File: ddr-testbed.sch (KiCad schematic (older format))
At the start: 23 parts, among them J1 ddr4-sodimm-edge-connector, U1 MT53E256M16D1

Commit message: Add changes refering to Xilinx documentation
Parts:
- added C?: C_10n_0402, antmicro-footprints:0402-cap, symbol antmicroCapacitors0402:C_10n_0402
- added R? (x4): R_0R_0402, antmicro-footprints:0402-res, symbol antmicroResistors0402:R_0R_0402
- added R? (x19): R_40R2_0402, antmicro-footprints:0402-res, symbol antmicroResistors0402:R_40R2_0402
- added R?: R_80R6_0402, antmicro-footprints:0402-res, symbol antmicroResistors0402:R_80R6_0402
- added R?: R_4k7_0402, antmicro-footprints:0402-res, symbol antmicroResistors0402:R_4k7_0402
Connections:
- net CK0_C_A is gone; now on net CK0_C: U1.J9 (CK_C_A)
- net CK0_C_B is gone; now on net CK1_C: U1.P9 (CK_C_B)
- net CK0_T_A is gone; now on net CK0_T: U1.J8 (CK_T_A)
- net CK0_T_B is gone; now on net CK1_T: U1.P8 (CK_T_B)
- net ODT0_A is gone; now on net GND: U1.G2 (ODT_CA_A)
- net ODT0_B is gone; now on net GND: U1.T2 (ODT_CA_B)
- net VTT is gone; now on net GND: R?.1, R?.1, R?.1, R?.1, R?.1, R?.1, R?.1, R?.1, R?.1, R?.1, R?.1, R?.1, R?.1, R?.1
- net CA0_A: now also R?.1
- net CA0_B: now also J1.146, R?.1; no longer J1.127
- net CA1_A: now also R?.1
- net CA1_B: now also J1.120, R?.1; no longer J1.122
- net CA2_A: now also R?.1
- net CA2_B: now also J1.119, R?.1; no longer J1.125
- net CA3_A: now also R?.1
- net CA3_B: now also J1.158, R?.1; no longer J1.121
- net CA4_A: now also R?.1
- net CA4_B: now also J1.151, R?.1; no longer J1.146
- net CA5_A: now also R?.1
- net CA5_B: now also J1.156, R?.1; no longer J1.120
- net CK0_C: now also R?.1
- net CK0_T: now also R?.1
- net CK1_C: now also R?.1
- net CK1_T: now also R?.1
- net CKE0_A: now also R?.1
- net CKE0_B: now also R?.1
- net CS0_N_A: now also R?.1
- net CS0_N_B: now also R?.1
- net DDRVCC: now also C?.1, R?.1
- net GND: now also C?.2, R?.2, R?.2, R?.2, R?.2, R?.2, R?.2, R?.2, R?.2, R?.2, R?.2, R?.2, R?.2, R?.2, R?.2, R?.2, R?.2, R?.2, R?.2, R?.2, R?.2
- net RESET_CONN_N: now also R?.1
- net CKE_0: now reaches J1.109
- net CKE_0: now also R?.2, R?.2, R?.2
- new net CKE_0_A: R?.1
- new net CKE_0_B: R?.1
- new net CS_0_N: R?.1, R?.2, R?.2
- no-connect marks 16 -> 15
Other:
- note added: "Pull up or pull down?\n"
- note added: "TODO: Replace with R_40"
- note added: "TODO: Replace with R_80"
- note added: "What is taht pin?"

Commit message: Add changes in pull ups and add missing components
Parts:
- removed C?: C_3p_0402, antmicro-footprints:0402-cap, symbol antmicroCapacitors0402:C_3p_0402
- removed R? (x14): R_33R_0402, antmicro-footprints:0402-res, symbol antmicroResistors0402:R_33R_0402
- removed R?: R_120R_0603, antmicro-footprints:0603-res, symbol antmicroResistors0603:R_120R_0603
- removed R?: R_39k_0402, antmicro-footprints:0402-res, symbol antmicroResistors0402:R_39k_0402
- removed R?: R_75R_0603, antmicro-footprints:0603-res, symbol antmicroResistors0603:R_75R_0603
- added C?: C_3p3_0402, antmicro-footprints:0402-res, symbol antmicroCapacitors0402:C_3p3_0402
- added R? (x4): R_0R_0402, antmicro-footprints:0402-res, symbol antmicroResistors0402:R_0R_0402
- added R? (x2): R_40R2_0402, antmicro-footprints:0402-res, symbol antmicroResistors0402:R_40R2_0402
- added R?: R_75R_0402, antmicro-footprints:0402-res, symbol antmicroResistors0402:R_75R_0402
- added R?: R_120R_0402, antmicro-footprints:0402-res, symbol antmicroResistors0402:R_120R_0402
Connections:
- net ALERT_N: now also R?.1
- net CK0_C: now also C?.1
- net CK0_T: now also C?.2
- net CK1_C: now also R?.2
- net CK1_T: now also R?.1
- net CS_0_N: now also R?.1, R?.1; no longer R?.1, R?.2
- net DDRVCC: now also R?.2
- net GND: now also R?.2, R?.2; no longer U1.G2 (ODT_CA_A), U1.T2 (ODT_CA_B)
- net MEMRST_N: now also R?.2
- net ODT0: now also R?.2
- net RESET_CONN_N: now also R?.1
- net CS_1_N: now reaches J1.157
- net CS_1_N: now also R?.1, R?.2, R?.2
- net ODT1: now reaches J1.161
- net ODT1: now also R?.2
- net VDDSPD: now reaches J1.255
- net VPP: now reaches J1.257
- net VPP: now also J1.259
- net VTT: now reaches J1.258
- new net ODT0_A: R?.1, R?.1, R?.1, U1.G2 (ODT_CA_A), U1.T2 (ODT_CA_B)
- no-connect marks 15 -> 17
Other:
- note added: "Bank adress"
- note added: "Bank group\n"
- note added: "To check"
- note removed: "?"
- note removed: "TODO: Replace with 0402"
- note removed: "TODO: Replace with 39R"
- note removed: "TODO: Replace with C_3p3"
- note removed: "TODO: Replace with R_36"
- note removed: "TODO: Replace with R_40"
- note removed: "TODO: Replace with R_80"
- note removed: "TODO: replace with 0402\n"
- moved on the sheet: C?, J1B, R?

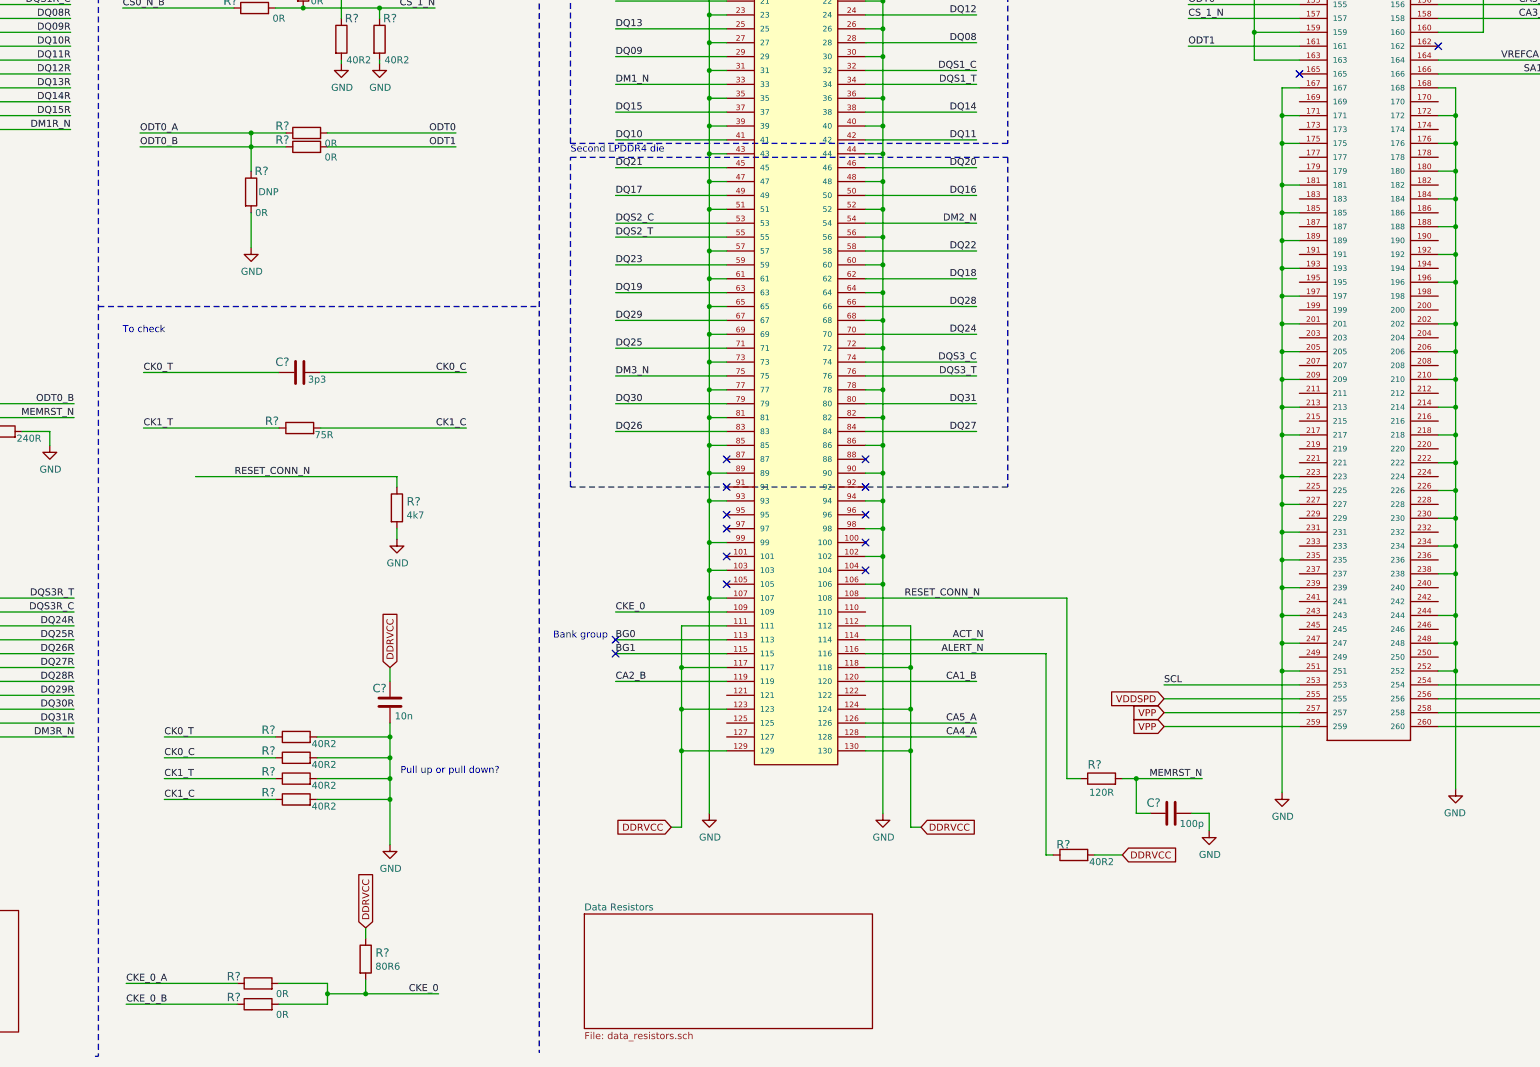
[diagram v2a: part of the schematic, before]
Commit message: Add changes around CKE pins and some notes
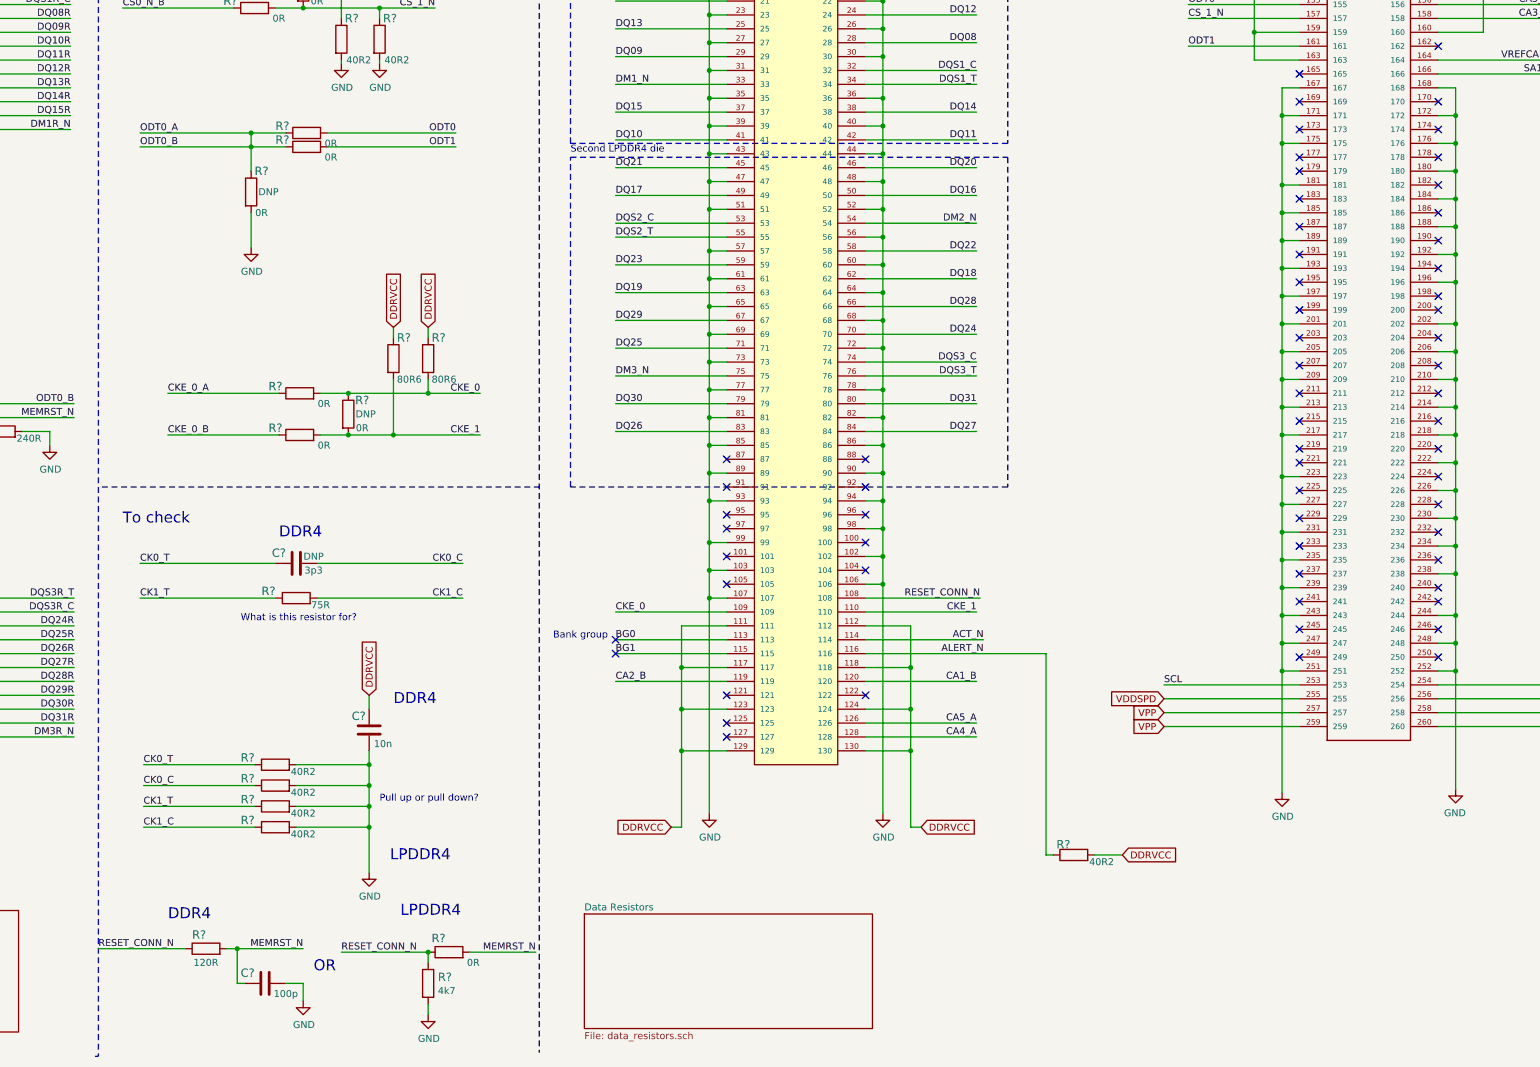
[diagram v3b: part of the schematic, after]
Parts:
- removed R? (x2): R_0R_0402, antmicro-footprints:0402-res, symbol antmicroResistors0402:R_0R_0402
- added R? (x4): R_0R_0402, antmicro-footprints:0402-res, symbol antmicroResistors0402:R_0R_0402
- added R?: R_80R6_0402, antmicro-footprints:0402-res, symbol antmicroResistors0402:R_80R6_0402
- C?: Populate (none) -> DNP
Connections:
- net CKE_0: now also R?.1, R?.2
- net CKE_0_A: now also R?.1
- net CKE_0_B: now also R?.1
- net DDRVCC: now also R?.1
- net MEMRST_N: now also R?.2
- net RESET_CONN_N: now also R?.1
- net CKE_1: now reaches J1.110
- net CKE_1: now also R?.2, R?.2, R?.2
- no-connect marks 17 -> 65
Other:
- note added: "DDR4"
- note added: "OR"
- note added: "What is this resistor for?"
- moved on the sheet: C?, R?

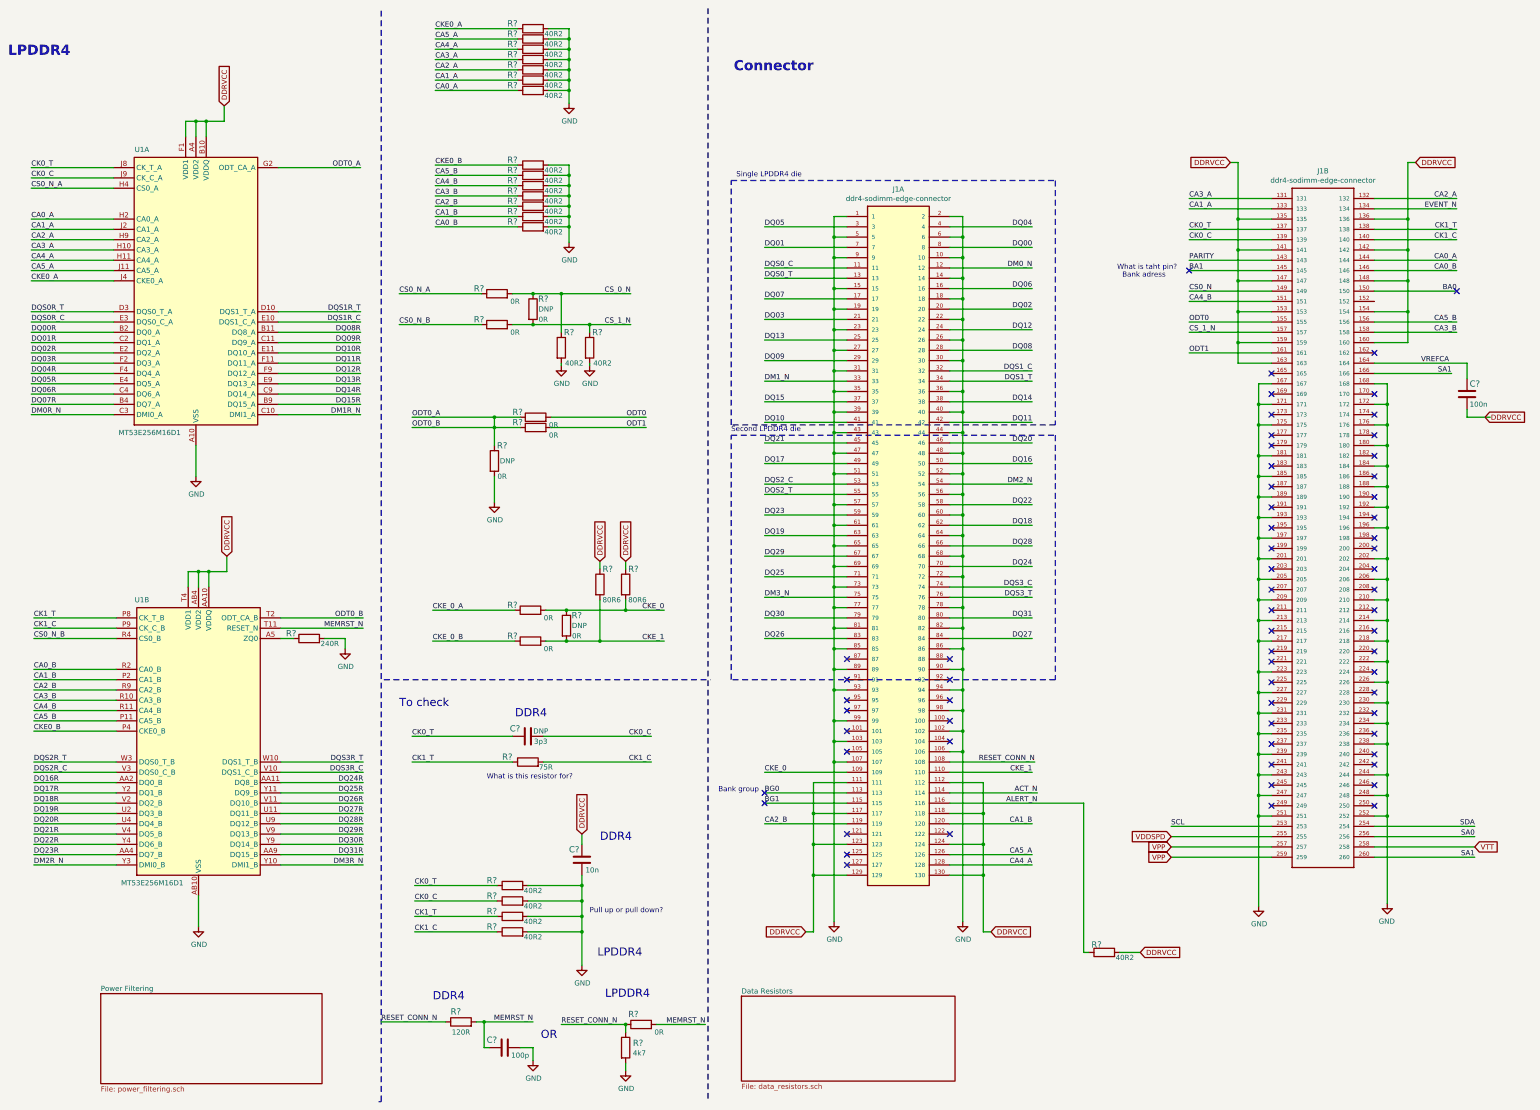
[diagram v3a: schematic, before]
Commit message: Remove data resistors sheet and add notes
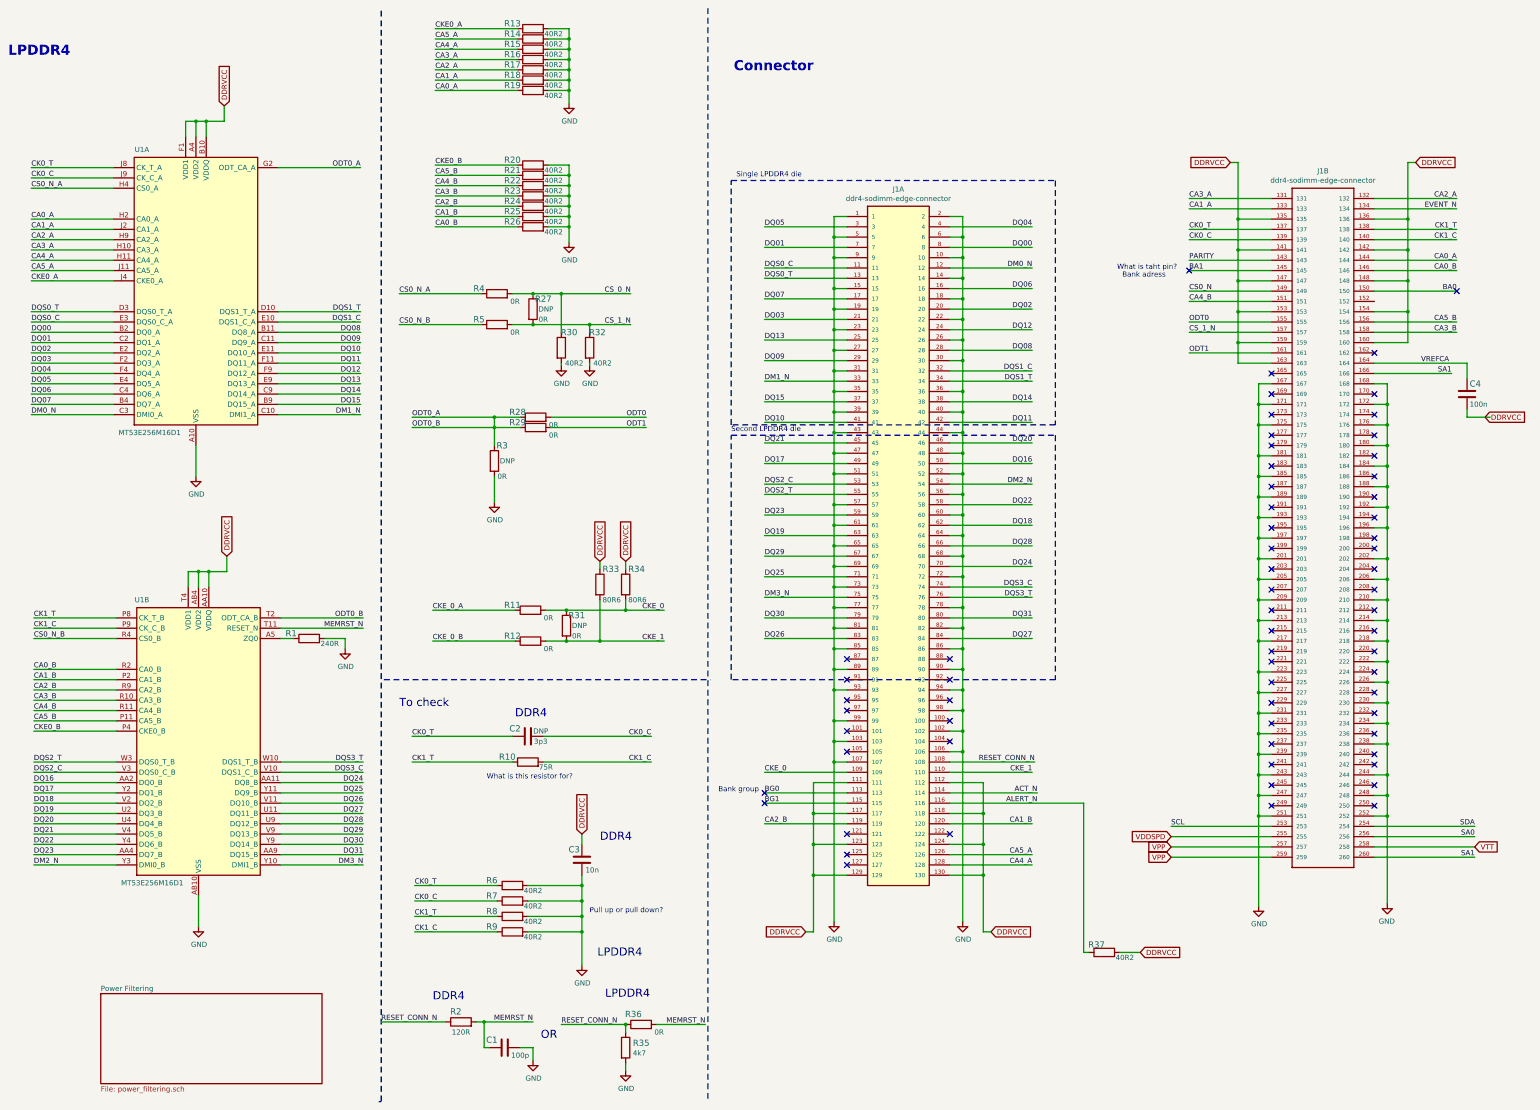
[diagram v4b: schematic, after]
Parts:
- gave numbers to parts that had none: 41
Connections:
- net DM0R_N is gone; now on net DM0_N: U1.C3 (DMI0_A)
- net DM1R_N is gone; now on net DM1_N: U1.C10 (DMI1_A)
- net DM2R_N is gone; now on net DM2_N: U1.Y3 (DMI0_B)
- net DM3R_N is gone; now on net DM3_N: U1.Y10 (DMI1_B)
- net DQ00R is gone; now on net DQ00: U1.B2 (DQ0_A)
- net DQ01R is gone; now on net DQ01: U1.C2 (DQ1_A)
- net DQ02R is gone; now on net DQ02: U1.E2 (DQ2_A)
- net DQ03R is gone; now on net DQ03: U1.F2 (DQ3_A)
- net DQ04R is gone; now on net DQ04: U1.F4 (DQ4_A)
- net DQ05R is gone; now on net DQ05: U1.E4 (DQ5_A)
- net DQ06R is gone; now on net DQ06: U1.C4 (DQ6_A)
- net DQ07R is gone; now on net DQ07: U1.B4 (DQ7_A)
- net DQ08R is gone; now on net DQ08: U1.B11 (DQ8_A)
- net DQ09R is gone; now on net DQ09: U1.C11 (DQ9_A)
- net DQ10R is gone; now on net DQ10: U1.E11 (DQ10_A)
- net DQ11R is gone; now on net DQ11: U1.F11 (DQ11_A)
- net DQ12R is gone; now on net DQ12: U1.F9 (DQ12_A)
- net DQ13R is gone; now on net DQ13: U1.E9 (DQ13_A)
- net DQ14R is gone; now on net DQ14: U1.C9 (DQ14_A)
- net DQ15R is gone; now on net DQ15: U1.B9 (DQ15_A)
- net DQ16R is gone; now on net DQ16: U1.AA2 (DQ0_B)
- net DQ17R is gone; now on net DQ17: U1.Y2 (DQ1_B)
- net DQ18R is gone; now on net DQ18: U1.V2 (DQ2_B)
- net DQ19R is gone; now on net DQ19: U1.U2 (DQ3_B)
- net DQ20R is gone; now on net DQ20: U1.U4 (DQ4_B)
- net DQ21R is gone; now on net DQ21: U1.V4 (DQ5_B)
- net DQ22R is gone; now on net DQ22: U1.Y4 (DQ6_B)
- net DQ23R is gone; now on net DQ23: U1.AA4 (DQ7_B)
- net DQ24R is gone; now on net DQ24: U1.AA11 (DQ8_B)
- net DQ25R is gone; now on net DQ25: U1.Y11 (DQ9_B)
- net DQ26R is gone; now on net DQ26: U1.V11 (DQ10_B)
- net DQ27R is gone; now on net DQ27: U1.U11 (DQ11_B)
- net DQ28R is gone; now on net DQ28: U1.U9 (DQ12_B)
- net DQ29R is gone; now on net DQ29: U1.V9 (DQ13_B)
- net DQ30R is gone; now on net DQ30: U1.Y9 (DQ14_B)
- net DQ31R is gone; now on net DQ31: U1.AA9 (DQ15_B)
- net DQS0R_C is gone; now on net DQS0_C: U1.E3 (DQS0_C_A)
- net DQS0R_T is gone; now on net DQS0_T: U1.D3 (DQS0_T_A)
- net DQS1R_C is gone; now on net DQS1_C: U1.E10 (DQS1_C_A)
- net DQS1R_T is gone; now on net DQS1_T: U1.D10 (DQS1_T_A)
- net DQS2R_C is gone; now on net DQS2_C: U1.V3 (DQS0_C_B)
- net DQS2R_T is gone; now on net DQS2_T: U1.W3 (DQS0_T_B)
- net DQS3R_C is gone; now on net DQS3_C: U1.V10 (DQS1_C_B)
- net DQS3R_T is gone; now on net DQS3_T: U1.W10 (DQS1_T_B)
